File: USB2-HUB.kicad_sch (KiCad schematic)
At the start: 32 parts, among them J11 USB_OTG, J13 690-008-221-904, J14 Conn_02x05_Odd_Even, U13 FSUSB42MUX, U4 TPD4EUSB30, U6 USB2514B-I/M2, U7 AP22653W6, Y1 24MHz

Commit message: removed HDMI, CAM and DISP1 connectors
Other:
- company: © 2020-2022 Raspberry Pi Ltd (formerly Raspberry Pi (Trading) Ltd.) -> (none)
- title: Compute Module 4 IO Board - USB -> Bitcart
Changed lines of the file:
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@@
   (paper "A4")
   (title_block
-    (title "Compute Module 4 IO Board - USB")
+    (title "Bitcart")
+    (date "2023-09-15")
     (rev "1")
-    (company "© 2020-2022 Raspberry Pi Ltd (formerly Raspberry Pi (Trading) Ltd.)")
-    (comment 1 "www.raspberrypi.com")
   )
   (junction (at 103.378 165.1) (diameter 1.016) (color 0 0 0 0)

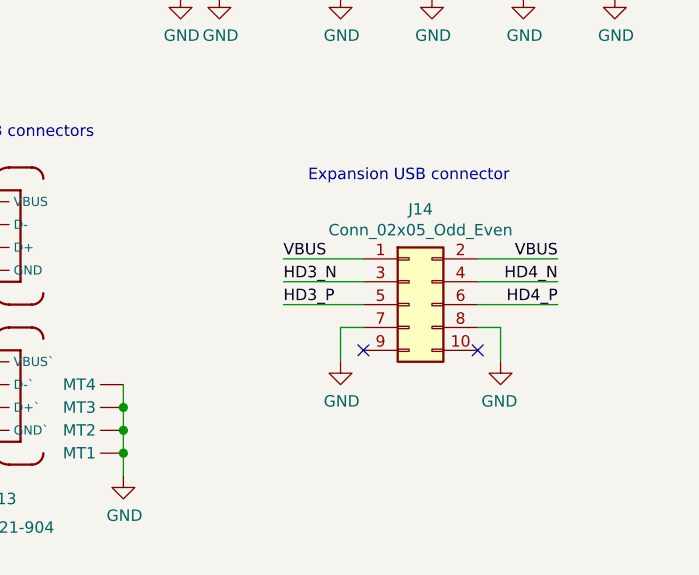
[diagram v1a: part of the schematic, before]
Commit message: extended the board to make room for IO connectors. added the vertical display connector.
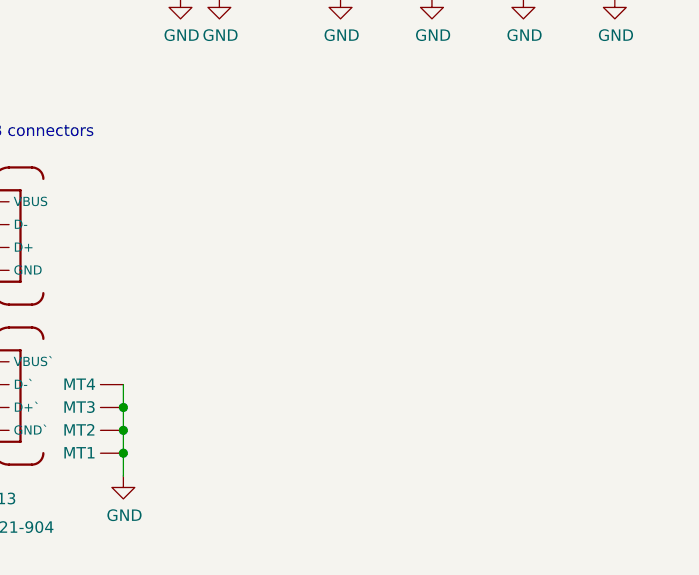
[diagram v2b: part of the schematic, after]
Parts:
- removed J14: Conn_02x05_Odd_Even, Connector_PinHeader_2.54mm:PinHeader_2x05_P2.54mm_Vertical, symbol Connector_Generic:Conn_02x05_Odd_Even
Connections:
- no-connect marks 9 -> 7
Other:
- note removed: "Expansion USB connector"
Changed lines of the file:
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@@
   (no_connect (at 95.25 104.14))
   (no_connect (at 120.65 44.45))
-  (no_connect (at 246.38 127))
-  (no_connect (at 259.08 127))
   (no_connect (at 95.25 124.46))
   (no_connect (at 151.13 119.38))
@@
     (stroke (width 0) (type solid))
   )
-  (wire (pts (xy 267.97 121.92) (xy 259.08 121.92))
-    (stroke (width 0) (type solid))
-  )
   (wire (pts (xy 151.13 88.9) (xy 160.02 88.9))
     (stroke (width 0) (type solid))
@@
     (stroke (width 0) (type solid))
   )
-  (wire (pts (xy 267.97 116.84) (xy 259.08 116.84))
-    (stroke (width 0) (type solid))
-  )
-  (wire (pts (xy 237.49 116.84) (xy 246.38 116.84))
-    (stroke (width 0) (type solid))
-  )
   (wire (pts (xy 151.13 91.44) (xy 160.02 91.44))
     (stroke (width 0) (type solid))
@@
     (stroke (width 0) (type solid))
   )
-  (wire (pts (xy 261.62 124.46) (xy 261.62 128.27))
-    (stroke (width 0) (type solid))
-  )
   (wire (pts (xy 214.63 45.72) (xy 231.14 45.72))
     (stroke (width 0) (type solid))
@@
     (stroke (width 0) (type solid))
   )
-  (wire (pts (xy 237.49 121.92) (xy 246.38 121.92))
-    (stroke (width 0) (type solid))
-  )
   (wire (pts (xy 219.71 133.35) (xy 219.71 135.89))
     (stroke (width 0) (type solid))
@@
     (stroke (width 0) (type solid))
   )
-  (wire (pts (xy 237.49 119.38) (xy 246.38 119.38))
-    (stroke (width 0) (type solid))
-  )
   (wire (pts (xy 103.378 165.1) (xy 116.84 165.1))
     (stroke (width 0) (type solid))
@@
     (stroke (width 0) (type solid))
   )
-  (wire (pts (xy 259.08 124.46) (xy 261.62 124.46))
-    (stroke (width 0) (type solid))
-  )
   (wire (pts (xy 63.5 58.42) (xy 74.93 58.42))
     (stroke (width 0) (type solid))
@@
     (stroke (width 0) (type solid))
   )
-  (wire (pts (xy 243.84 124.46) (xy 246.38 124.46))
-    (stroke (width 0) (type solid))
-  )
   (wire (pts (xy 74.93 172.72) (xy 84.074 172.72))
     (stroke (width 0) (type solid))
@@
     (stroke (width 0) (type solid))
   )
-  (wire (pts (xy 243.84 124.46) (xy 243.84 128.27))
-    (stroke (width 0) (type solid))
-  )
   (wire (pts (xy 116.84 165.1) (xy 128.27 165.1))
     (stroke (width 0) (type solid))
@@
     (stroke (width 0) (type solid))
   )
-  (wire (pts (xy 267.97 119.38) (xy 259.08 119.38))
-    (stroke (width 0) (type solid))
-  )
   (wire (pts (xy 46.99 134.62) (xy 46.99 137.16))
     (stroke (width 0) (type solid))
@@
   (wire (pts (xy 243.84 80.01) (xy 243.84 77.47))
     (stroke (width 0) (type solid))
-  )
-  (text "Expansion USB connector" (at 262.6106 108.3818 0)
-    (effects (font (size 1.27 1.27)) (justify right bottom))
   )
   (text "Current Limit switch" (at 212.09 68.58 0)
@@
     (effects (font (size 1.27 1.27)) (justify left bottom))
   )
-  (label "HD3_N" (at 237.49 119.38 0) (fields_autoplaced)
-    (effects (font (size 1.27 1.27)) (justify left bottom))
-  )
   (label "HD1_P" (at 190.5 133.35 0) (fields_autoplaced)
     (effects (font (size 1.27 1.27)) (justify left bottom))
@@
   )
   (label "HD4_P" (at 154.94 129.54 0) (fields_autoplaced)
-    (effects (font (size 1.27 1.27)) (justify left bottom))
-  )
-  (label "VBUS" (at 237.49 116.84 0) (fields_autoplaced)
     (effects (font (size 1.27 1.27)) (justify left bottom))
   )
@@
     (effects (font (size 1.27 1.27)) (justify left bottom))
   )
-  (label "HD4_P" (at 267.97 121.92 180) (fields_autoplaced)
-    (effects (font (size 1.27 1.27)) (justify right bottom))
-  )
   (label "USBH_P" (at 81.28 96.52 0) (fields_autoplaced)
     (effects (font (size 1.27 1.27)) (justify left bottom))
@@
     (effects (font (size 1.27 1.27)) (justify left bottom))
   )
-  (label "HD4_N" (at 267.97 119.38 180) (fields_autoplaced)
-    (effects (font (size 1.27 1.27)) (justify right bottom))
-  )
   (label "nOCS1" (at 154.94 134.62 0) (fields_autoplaced)
     (effects (font (size 1.27 1.27)) (justify left bottom))
@@
     (effects (font (size 1.27 1.27)) (justify left bottom))
   )
-  (label "HD3_P" (at 237.49 121.92 0) (fields_autoplaced)
-    (effects (font (size 1.27 1.27)) (justify left bottom))
-  )
   (label "PWR1" (at 187.96 82.55 0) (fields_autoplaced)
     (effects (font (size 1.27 1.27)) (justify left bottom))
@@
   (label "HD1_P" (at 154.94 91.44 0) (fields_autoplaced)
     (effects (font (size 1.27 1.27)) (justify left bottom))
-  )
-  (label "VBUS" (at 267.97 116.84 180) (fields_autoplaced)
-    (effects (font (size 1.27 1.27)) (justify right bottom))
   )
   (hierarchical_label "USB2_N" (shape bidirectional) (at 27.94 64.77 180) (fields_autoplaced)
@@
         )
       )
-    )
-  )
-  (symbol (lib_id "power:GND") (at 243.84 128.27 0) (unit 1)
-    (in_bom yes) (on_board yes) (dnp no)
-    (property "Reference" "#PWR025" (at 243.84 134.62 0)
-      (effects (font (size 1.27 1.27)) hide)
-    )
-    (property "Value" "GND" (at 243.967 132.6642 0)
-      (effects (font (size 1.27 1.27)))
-    )
-    (property "Footprint" "" (at 243.84 128.27 0)
-      (effects (font (size 1.27 1.27)) hide)
-    )
-    (property "Datasheet" "" (at 243.84 128.27 0)
-      (effects (font (size 1.27 1.27)) hide)
-    )
-    (pin "1")
-    (instances
-      (project "bitcart"
-        (path "/e63e39d7-6ac0-4ffd-8aa3-1841a4541b55/00000000-0000-0000-0000-00005e072e02"
-          (reference "#PWR025") (unit 1)
-        )
-      )
-    )
-  )
-  (symbol (lib_id "power:GND") (at 261.62 128.27 0) (mirror y) (unit 1)
-    (in_bom yes) (on_board yes) (dnp no)
-    (property "Reference" "#PWR026" (at 261.62 134.62 0)
-      (effects (font (size 1.27 1.27)) hide)
-    )
-    (property "Value" "GND" (at 261.493 132.6642 0)
-      (effects (font (size 1.27 1.27)))
-    )
-    (property "Footprint" "" (at 261.62 128.27 0)
-      (effects (font (size 1.27 1.27)) hide)
-    )
-    (property "Datasheet" "" (at 261.62 128.27 0)
-      (effects (font (size 1.27 1.27)) hide)
-    )
-    (pin "1")
-    (instances
-      (project "bitcart"
-        (path "/e63e39d7-6ac0-4ffd-8aa3-1841a4541b55/00000000-0000-0000-0000-00005e072e02"
-          (reference "#PWR026") (unit 1)
-        )
-      )
-    )
-  )
-  (symbol (lib_id "Connector_Generic:Conn_02x05_Odd_Even") (at 251.46 121.92 0) (unit 1)
-    (in_bom yes) (on_board yes) (dnp no)
-    (property "Reference" "J14" (at 252.73 111.3282 0)
-      (effects (font (size 1.27 1.27)))
-    )
-    (property "Value" "Conn_02x05_Odd_Even" (at 252.73 113.6396 0)
-      (effects (font (size 1.27 1.27)))
-    )
-    (property "Footprint" "Connector_PinHeader_2.54mm:PinHeader_2x05_P2.54mm_Vertical" (at 251.46 121.92 0)
-      (effects (font (size 1.27 1.27)) hide)
-    )
-    (property "Datasheet" "https://www.toby.co.uk/uploads/publications/1673.pdf" (at 251.46 121.92 0)
-      (effects (font (size 1.27 1.27)) hide)
-    )
-    (property "Field4" "Toby" (at 251.46 121.92 0)
-      (effects (font (size 1.27 1.27)) hide)
-    )
-    (property "Field5" "THD-05-R" (at 251.46 121.92 0)
-      (effects (font (size 1.27 1.27)) hide)
-    )
-    (property "Field6" "THD-05-R" (at 251.46 121.92 0)
-      (effects (font (size 1.27 1.27)) hide)
-    )
-    (property "Field7" "Toby" (at 251.46 121.92 0)
-      (effects (font (size 1.27 1.27)) hide)
-    )
-    (property "Part Description" "PinHeader_2x05_P2.54mm_Vertical" (at 251.46 121.92 0)
-      (effects (font (size 1.27 1.27)) hide)
-    )
-    (pin "1")
-    (pin "10")
-    (pin "2")
-    (pin "3")
-    (pin "4")
-    (pin "5")
-    (pin "6")
-    (pin "7")
-    (pin "8")
-    (pin "9")
-    (instances
-      (project "bitcart"
-        (path "/e63e39d7-6ac0-4ffd-8aa3-1841a4541b55/00000000-0000-0000-0000-00005e072e02"
-          (reference "J14") (unit 1)
-        )
-      )
